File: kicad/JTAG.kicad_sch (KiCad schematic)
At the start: 1 part, among them J2 TC2030

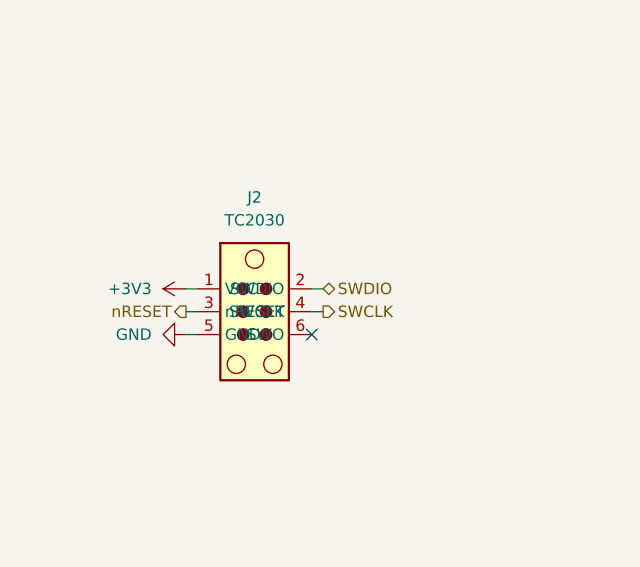
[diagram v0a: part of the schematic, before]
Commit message: feat: remake power management and use the same as the reference DK
Signed-off-by: Bobo Bäck Engström <bobo@id8-engineering.io>
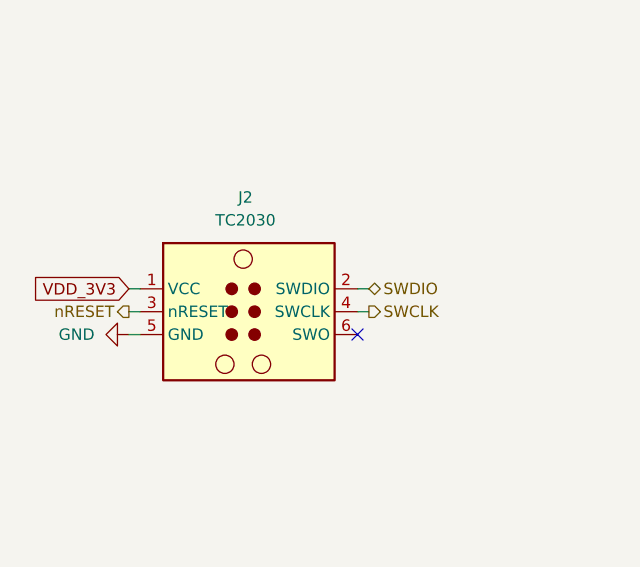
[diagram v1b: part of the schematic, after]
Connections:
- net +3V3 renamed VDD_3V3
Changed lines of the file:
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@@
 	)
 	(no_connect
-		(at 99.06 97.79)
-	)
-	(wire
-		(pts
-			(xy 100.33 92.71) (xy 99.06 92.71)
-		)
-		(stroke
-			(width 0)
-			(type default)
-		)
-	)
-	(wire
-		(pts
-			(xy 100.33 95.25) (xy 99.06 95.25)
-		)
-		(stroke
-			(width 0)
-			(type default)
-		)
-	)
-	(wire
-		(pts
-			(xy 85.09 97.79) (xy 86.36 97.79)
-		)
-		(stroke
-			(width 0)
-			(type default)
-		)
-	)
-	(wire
-		(pts
-			(xy 85.09 92.71) (xy 86.36 92.71)
+		(at 104.14 97.79)
+	)
+	(wire
+		(pts
+			(xy 105.41 95.25) (xy 104.14 95.25)
+		)
+		(stroke
+			(width 0)
+			(type default)
+		)
+	)
+	(wire
+		(pts
+			(xy 105.41 92.71) (xy 104.14 92.71)
+		)
+		(stroke
+			(width 0)
+			(type default)
+		)
+	)
+	(wire
+		(pts
+			(xy 78.74 97.79) (xy 80.01 97.79)
 		)
 		(stroke
@@
 	(wire
 		(pts
-			(xy 85.09 95.25) (xy 86.36 95.25)
-		)
-		(stroke
-			(width 0)
-			(type default)
+			(xy 78.74 92.71) (xy 80.01 92.71)
+		)
+		(stroke
+			(width 0)
+			(type default)
+		)
+	)
+	(wire
+		(pts
+			(xy 78.74 95.25) (xy 80.01 95.25)
+		)
+		(stroke
+			(width 0)
+			(type default)
+		)
+	)
+	(global_label "VDD_3V3"
+		(shape input)
+		(at 78.74 92.71 180)
+		(fields_autoplaced yes)
+		(effects
+			(font
+				(size 1.27 1.27)
+			)
+			(justify right)
+		)
+		(property "Intersheetrefs" "${INTERSHEET_REFS}"
+			(at 67.651 92.71 0)
+			(effects
+				(font
+					(size 1.27 1.27)
+				)
+				(justify right)
+				(hide yes)
+			)
 		)
 	)
 	(hierarchical_label "SWDIO"
 		(shape bidirectional)
-		(at 100.33 92.71 0)
+		(at 105.41 92.71 0)
 		(effects
 			(font
@@
 			)
 			(justify left)
+		)
+	)
+	(hierarchical_label "nRESET"
+		(shape output)
+		(at 78.74 95.25 180)
+		(effects
+			(font
+				(size 1.27 1.27)
+			)
+			(justify right)
 		)
 	)
 	(hierarchical_label "SWCLK"
 		(shape output)
-		(at 100.33 95.25 0)
+		(at 105.41 95.25 0)
 		(effects
 			(font
@@
 		)
 	)
-	(hierarchical_label "nRESET"
-		(shape output)
-		(at 85.09 95.25 180)
-		(effects
-			(font
-				(size 1.27 1.27)
-			)
-			(justify right)
-		)
-	)
 	(symbol
+		(lib_name "TC2030_1")
 		(lib_id "seven_lib:TC2030")
-		(at 91.44 95.25 0)
+		(at 90.17 95.25 0)
 		(unit 1)
 		(exclude_from_sim no)
@@
 		(fields_autoplaced yes)
 		(property "Reference" "J2"
-			(at 92.71 82.55 0)
+			(at 91.694 82.55 0)
 			(effects
 				(font
@@
 		)
 		(property "Value" "TC2030"
-			(at 92.71 85.09 0)
+			(at 91.694 85.09 0)
 			(effects
 				(font
@@
 		)
 		(property "Footprint" "seven-lib:Tag-Connect_TC2030-IDC-NL_2x03_P1.27mm_Vertical"
-			(at 92.71 95.25 0)
+			(at 91.44 95.25 0)
 			(effects
 				(font
@@
 		)
 		(property "Datasheet" "https://www.tag-connect.com/wp-content/uploads/bsk-pdf-manager/2019/12/TC2030-IDC-NL-Datasheet-Rev-B.pdf"
-			(at 92.71 95.25 0)
+			(at 91.44 95.25 0)
 			(effects
 				(font
@@
 		)
 		(property "Description" "Tag-Connect’s 6-pins connector"
-			(at 91.44 95.25 0)
-			(effects
-				(font
-					(size 1.27 1.27)
-				)
-				(hide yes)
-			)
+			(at 90.17 95.25 0)
+			(effects
+				(font
+					(size 1.27 1.27)
+				)
+				(hide yes)
+			)
+		)
+		(pin "3"
+		)
+		(pin "1"
+		)
+		(pin "6"
 		)
 		(pin "4"
-		)
-		(pin "6"
-		)
-		(pin "3"
-		)
-		(pin "1"
 		)
 		(pin "2"
@@
 	)
 	(symbol
-		(lib_id "seven_lib:+3V3")
-		(at 85.09 92.71 90)
-		(unit 1)
-		(exclude_from_sim no)
-		(in_bom yes)
-		(on_board yes)
-		(dnp no)
-		(fields_autoplaced yes)
-		(property "Reference" "#PWR04"
-			(at 88.9 92.71 0)
-			(effects
-				(font
-					(size 1.27 1.27)
-				)
-				(hide yes)
-			)
-		)
-		(property "Value" "+3V3"
-			(at 81.28 92.7099 90)
-			(effects
-				(font
-					(size 1.27 1.27)
-				)
-				(justify left)
-			)
-		)
-		(property "Footprint" ""
-			(at 85.09 92.71 0)
-			(effects
-				(font
-					(size 1.27 1.27)
-				)
-				(hide yes)
-			)
-		)
-		(property "Datasheet" ""
-			(at 85.09 92.71 0)
-			(effects
-				(font
-					(size 1.27 1.27)
-				)
-				(hide yes)
-			)
-		)
-		(property "Description" "Power symbol creates a global label with name \"+3V3\""
-			(at 85.09 92.71 0)
-			(effects
-				(font
-					(size 1.27 1.27)
-				)
-				(hide yes)
-			)
-		)
-		(pin "1"
-		)
-		(instances
-			(project ""
-				(path "/8e3cc843-5797-49f3-8b3a-1c11450ccd1e/05f18bcb-1f58-4fb2-bbec-23b1ba834d60"
-					(reference "#PWR04")
-					(unit 1)
-				)
-			)
-		)
-	)
-	(symbol
 		(lib_id "seven_lib:GND")
-		(at 85.09 97.79 270)
+		(at 78.74 97.79 270)
 		(unit 1)
 		(exclude_from_sim no)
@@
 		(fields_autoplaced yes)
 		(property "Reference" "#PWR05"
+			(at 72.39 97.79 0)
+			(effects
+				(font
+					(size 1.27 1.27)
+				)
+				(hide yes)
+			)
+		)
+		(property "Value" "GND"
+			(at 74.93 97.7899 90)
+			(effects
+				(font
+					(size 1.27 1.27)
+				)
+				(justify right)
+			)
+		)
+		(property "Footprint" ""
 			(at 78.74 97.79 0)
 			(effects
@@
 			)
 		)
-		(property "Value" "GND"
-			(at 81.28 97.7899 90)
-			(effects
-				(font
-					(size 1.27 1.27)
-				)
-				(justify right)
-			)
-		)
-		(property "Footprint" ""
-			(at 85.09 97.79 0)
-			(effects
-				(font
-					(size 1.27 1.27)
-				)
-				(hide yes)
-			)
-		)
 		(property "Datasheet" ""
-			(at 85.09 97.79 0)
+			(at 78.74 97.79 0)
 			(effects
 				(font
@@
 		)
 		(property "Description" "Power symbol creates a global label with name \"GND\" , ground"
-			(at 85.09 97.79 0)
+			(at 78.74 97.79 0)
 			(effects
 				(font
@@
 		)
 		(instances
-			(project ""
+			(project "seven"
 				(path "/8e3cc843-5797-49f3-8b3a-1c11450ccd1e/05f18bcb-1f58-4fb2-bbec-23b1ba834d60"
 					(reference "#PWR05")

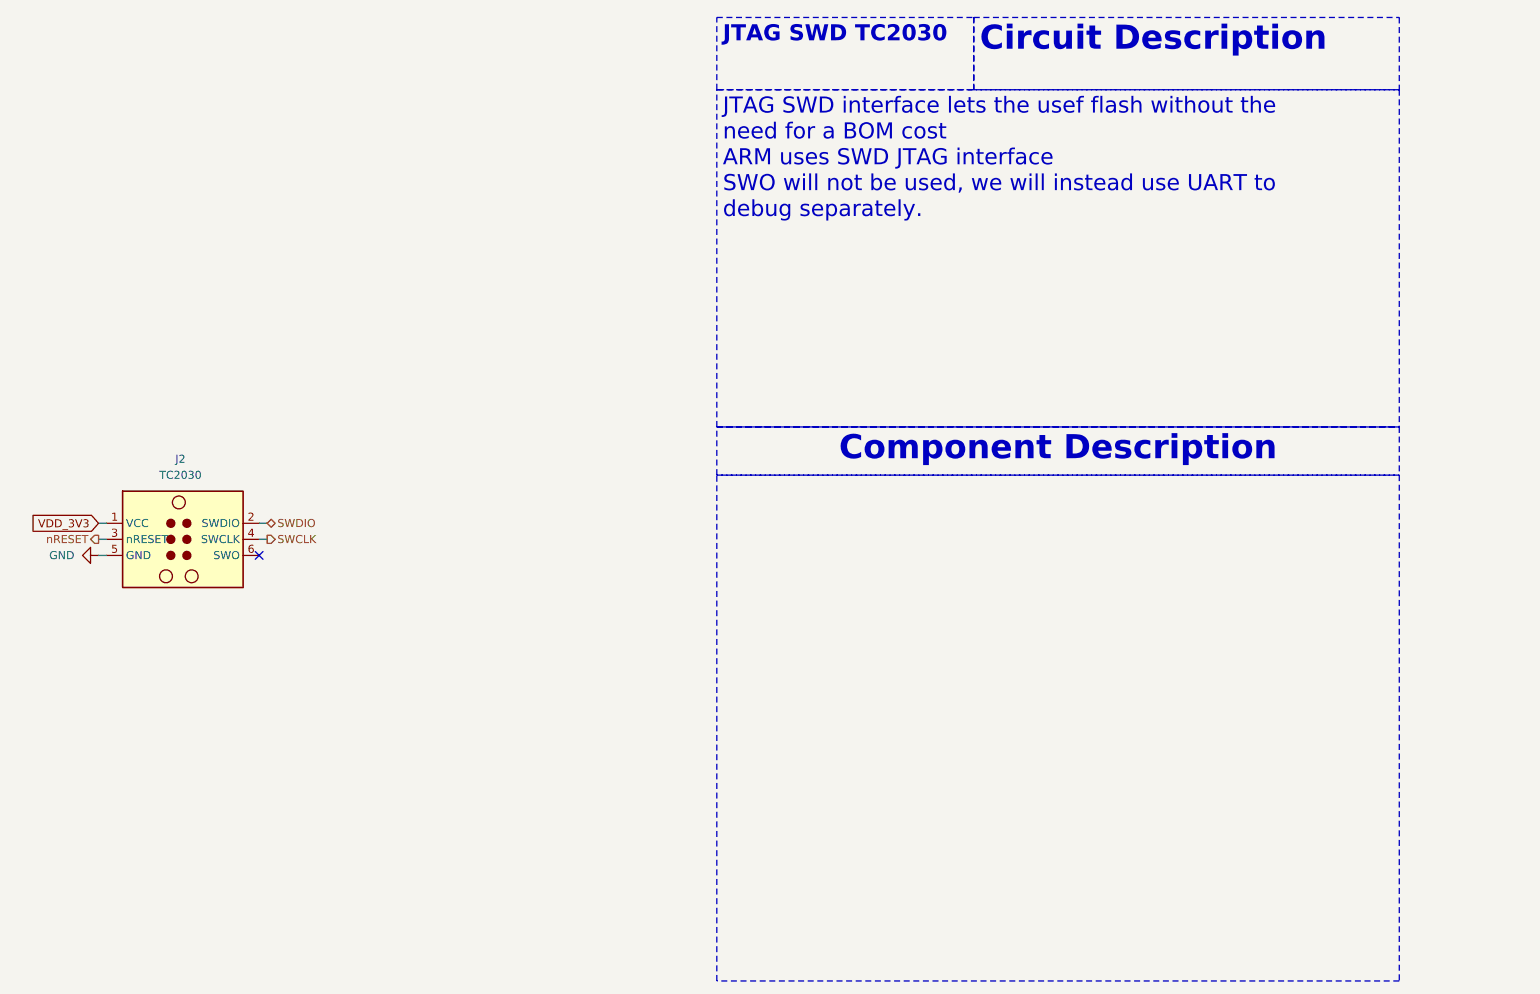
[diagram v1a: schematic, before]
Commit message: docs: update documentation to be more accurate
Signed-off-by: Bobo Bäck Engström <bobo@id8-engineering.io>
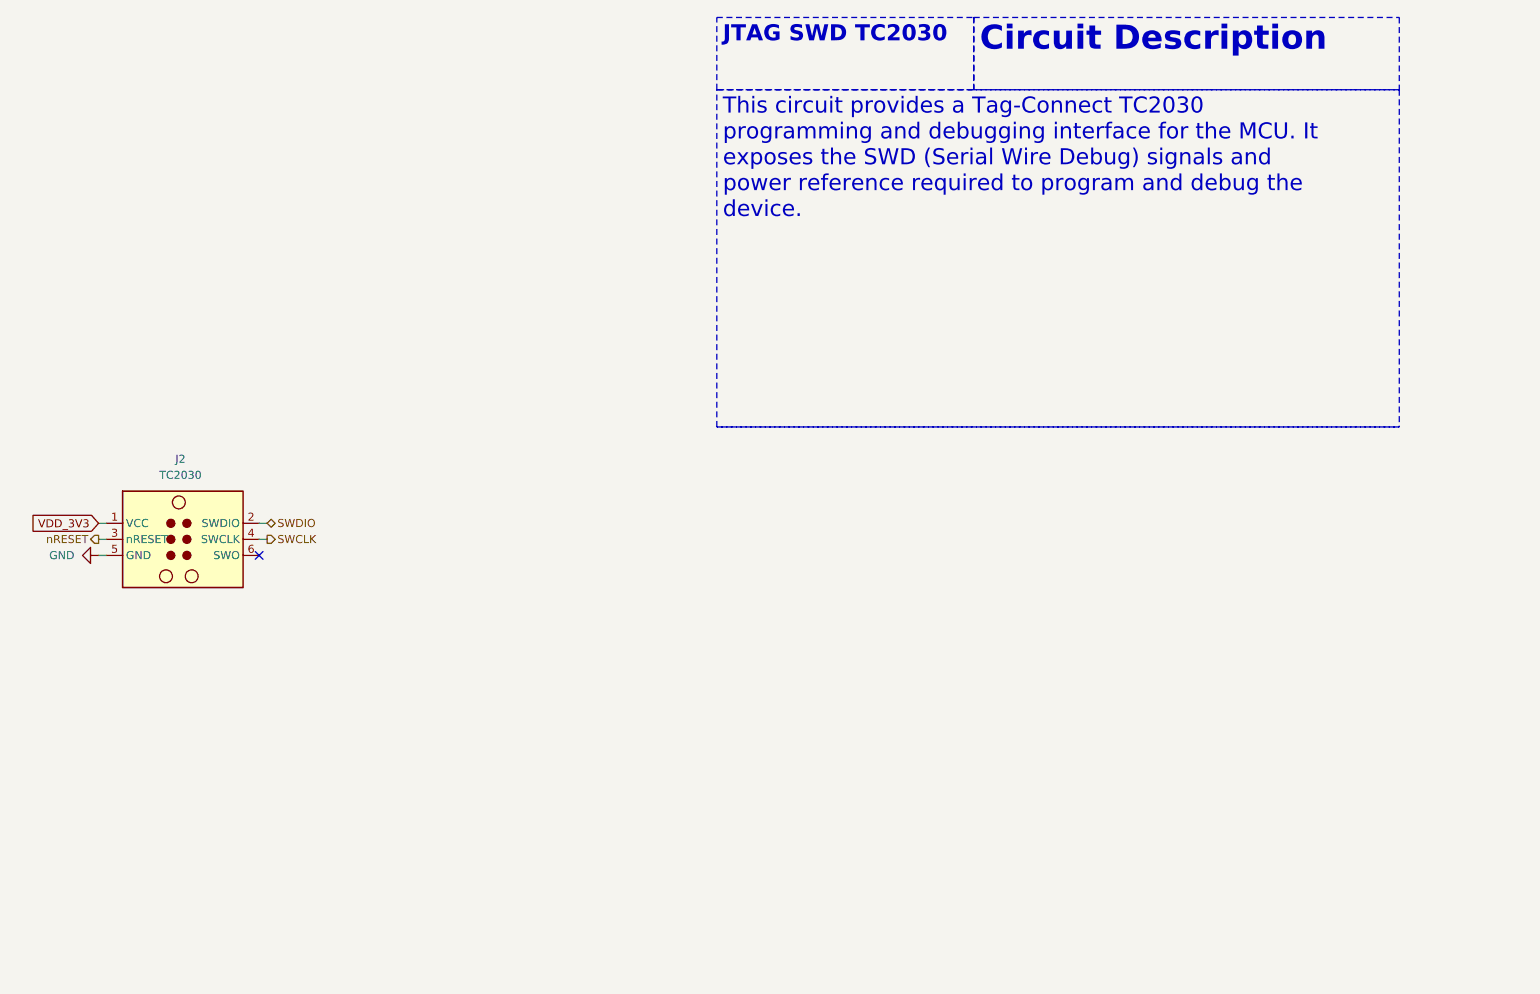
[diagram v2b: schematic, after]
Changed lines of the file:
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@@
 		)
 	)
-	(text_box "JTAG SWD interface lets the usef flash without the need for a BOM cost\nARM uses SWD JTAG interface\nSWO will not be used, we will instead use UART to debug separately. "
+	(text_box "This circuit provides a Tag-Connect TC2030 programming and debugging interface for the MCU. It exposes the SWD (Serial Wire Debug) signals and power reference required to program and debug the device."
 		(exclude_from_sim no)
 		(at 176.53 24.13 0)
@@
 		)
 	)
-	(text_box "\n"
-		(exclude_from_sim no)
-		(at 176.53 85.09 0)
-		(size 107.95 80.01)
-		(margins 0.9525 0.9525 0.9525 0.9525)
-		(stroke
-			(width 0)
-			(type dash)
-		)
-		(fill
-			(type none)
-		)
-		(effects
-			(font
-				(size 2.54 2.54)
-			)
-			(justify left top)
-		)
-	)
-	(text_box "Component Description\n"
-		(exclude_from_sim no)
-		(at 176.53 77.47 0)
-		(size 107.95 7.62)
-		(margins 0.9525 0.9525 0.9525 0.9525)
-		(stroke
-			(width 0)
-			(type dash)
-		)
-		(fill
-			(type none)
-		)
-		(effects
-			(font
-				(size 3.81 3.81)
-				(thickness 0.762)
-				(bold yes)
-			)
-			(justify top)
-		)
-	)

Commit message: fix: changes made according to review meeting
Signed-off-by: Bobo Bäck Engström <bobo@id8-engineering.io>
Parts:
- added TP10: SWCLK, seven-lib:TestPoint_Pad_2.0x2.0mm, symbol seven_lib:TestPoint
- added TP9: SWDIO, seven-lib:TestPoint_Pad_2.0x2.0mm, symbol seven_lib:TestPoint
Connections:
- net SWCLK: now also TP10.1
- net SWDIO: now also TP9.1
- net VDD_3V3 renamed VDD_JTAG
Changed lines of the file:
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@@
 		)
+	)
+	(junction
+		(at 107.95 92.71)
+		(diameter 0)
+		(color 0 0 0 0)
+	)
+	(junction
+		(at 107.95 95.25)
+		(diameter 0)
+		(color 0 0 0 0)
 	)
 	(no_connect
@@
 	(wire
 		(pts
-			(xy 105.41 95.25) (xy 104.14 95.25)
-		)
-		(stroke
-			(width 0)
-			(type default)
-		)
-	)
-	(wire
-		(pts
-			(xy 105.41 92.71) (xy 104.14 92.71)
+			(xy 109.22 95.25) (xy 107.95 95.25)
+		)
+		(stroke
+			(width 0)
+			(type default)
+		)
+	)
+	(wire
+		(pts
+			(xy 107.95 95.25) (xy 104.14 95.25)
+		)
+		(stroke
+			(width 0)
+			(type default)
+		)
+	)
+	(wire
+		(pts
+			(xy 107.95 77.47) (xy 107.95 92.71)
+		)
+		(stroke
+			(width 0)
+			(type default)
+		)
+	)
+	(wire
+		(pts
+			(xy 109.22 92.71) (xy 107.95 92.71)
 		)
 		(stroke
@@
 		)
 	)
+	(wire
+		(pts
+			(xy 107.95 102.87) (xy 107.95 95.25)
+		)
+		(stroke
+			(width 0)
+			(type default)
+		)
+	)
 	(polyline
 		(pts
@@
 	(wire
 		(pts
+			(xy 104.14 92.71) (xy 107.95 92.71)
+		)
+		(stroke
+			(width 0)
+			(type default)
+		)
+	)
+	(wire
+		(pts
 			(xy 78.74 92.71) (xy 80.01 92.71)
 		)
@@
 		)
 	)
-	(global_label "VDD_3V3"
+	(global_label "VDD_JTAG"
 		(shape input)
 		(at 78.74 92.71 180)
@@
 		)
 		(property "Intersheetrefs" "${INTERSHEET_REFS}"
-			(at 67.651 92.71 0)
+			(at 66.8648 92.71 0)
 			(effects
 				(font
@@
 	(hierarchical_label "SWDIO"
 		(shape bidirectional)
-		(at 105.41 92.71 0)
+		(at 109.22 92.71 0)
 		(effects
 			(font
@@
 	(hierarchical_label "SWCLK"
 		(shape output)
-		(at 105.41 95.25 0)
+		(at 109.22 95.25 0)
 		(effects
 			(font
@@
 	)
 	(symbol
+		(lib_id "seven_lib:TestPoint")
+		(at 107.95 102.87 180)
+		(unit 1)
+		(exclude_from_sim no)
+		(in_bom yes)
+		(on_board yes)
+		(dnp no)
+		(property "Reference" "TP10"
+			(at 104.013 104.775 0)
+			(effects
+				(font
+					(size 1.27 1.27)
+				)
+			)
+		)
+		(property "Value" "SWCLK"
+			(at 104.013 107.315 0)
+			(effects
+				(font
+					(size 1.27 1.27)
+				)
+			)
+		)
+		(property "Footprint" "seven-lib:TestPoint_Pad_2.0x2.0mm"
+			(at 102.87 102.87 0)
+			(effects
+				(font
+					(size 1.27 1.27)
+				)
+				(hide yes)
+			)
+		)
+		(property "Datasheet" "~"
+			(at 102.87 102.87 0)
+			(effects
+				(font
+					(size 1.27 1.27)
+				)
+				(hide yes)
+			)
+		)
+		(property "Description" "test point"
+			(at 107.95 102.87 0)
+			(effects
+				(font
+					(size 1.27 1.27)
+				)
+				(hide yes)
+			)
+		)
+		(pin "1"
+		)
+		(instances
+			(project "seven"
+				(path "/8e3cc843-5797-49f3-8b3a-1c11450ccd1e/05f18bcb-1f58-4fb2-bbec-23b1ba834d60"
+					(reference "TP10")
+					(unit 1)
+				)
+			)
+		)
+	)
+	(symbol
 		(lib_id "seven_lib:GND")
 		(at 78.74 97.79 270)
@@
 					(unit 1)
 				)
+			)
+		)
+	)
+	(symbol
+		(lib_id "seven_lib:TestPoint")
+		(at 107.95 77.47 0)
+		(unit 1)
+		(exclude_from_sim no)
+		(in_bom yes)
+		(on_board yes)
+		(dnp no)
+		(property "Reference" "TP9"
+			(at 111.633 73.025 0)
+			(effects
+				(font
+					(size 1.27 1.27)
+				)
+			)
+		)
+		(property "Value" "SWDIO"
+			(at 111.633 75.565 0)
+			(effects
+				(font
+					(size 1.27 1.27)
+				)
+			)
+		)
+		(property "Footprint" "seven-lib:TestPoint_Pad_2.0x2.0mm"
+			(at 113.03 77.47 0)
+			(effects
+				(font
+					(size 1.27 1.27)
+				)
+				(hide yes)
+			)
+		)
+		(property "Datasheet" "~"
+			(at 113.03 77.47 0)
+			(effects
+				(font
+					(size 1.27 1.27)
+				)
+				(hide yes)
+			)
+		)
+		(property "Description" "test point"
+			(at 107.95 77.47 0)
+			(effects
+				(font
+					(size 1.27 1.27)
+				)
+				(hide yes)
+			)
+		)
+		(pin "1"
+		)
+		(instances
+			(project "seven"
+				(path "/8e3cc843-5797-49f3-8b3a-1c11450ccd1e/05f18bcb-1f58-4fb2-bbec-23b1ba834d60"
+					(reference "TP9")
+					(unit 1)
+				)
